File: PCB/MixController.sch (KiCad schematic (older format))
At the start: 20 parts

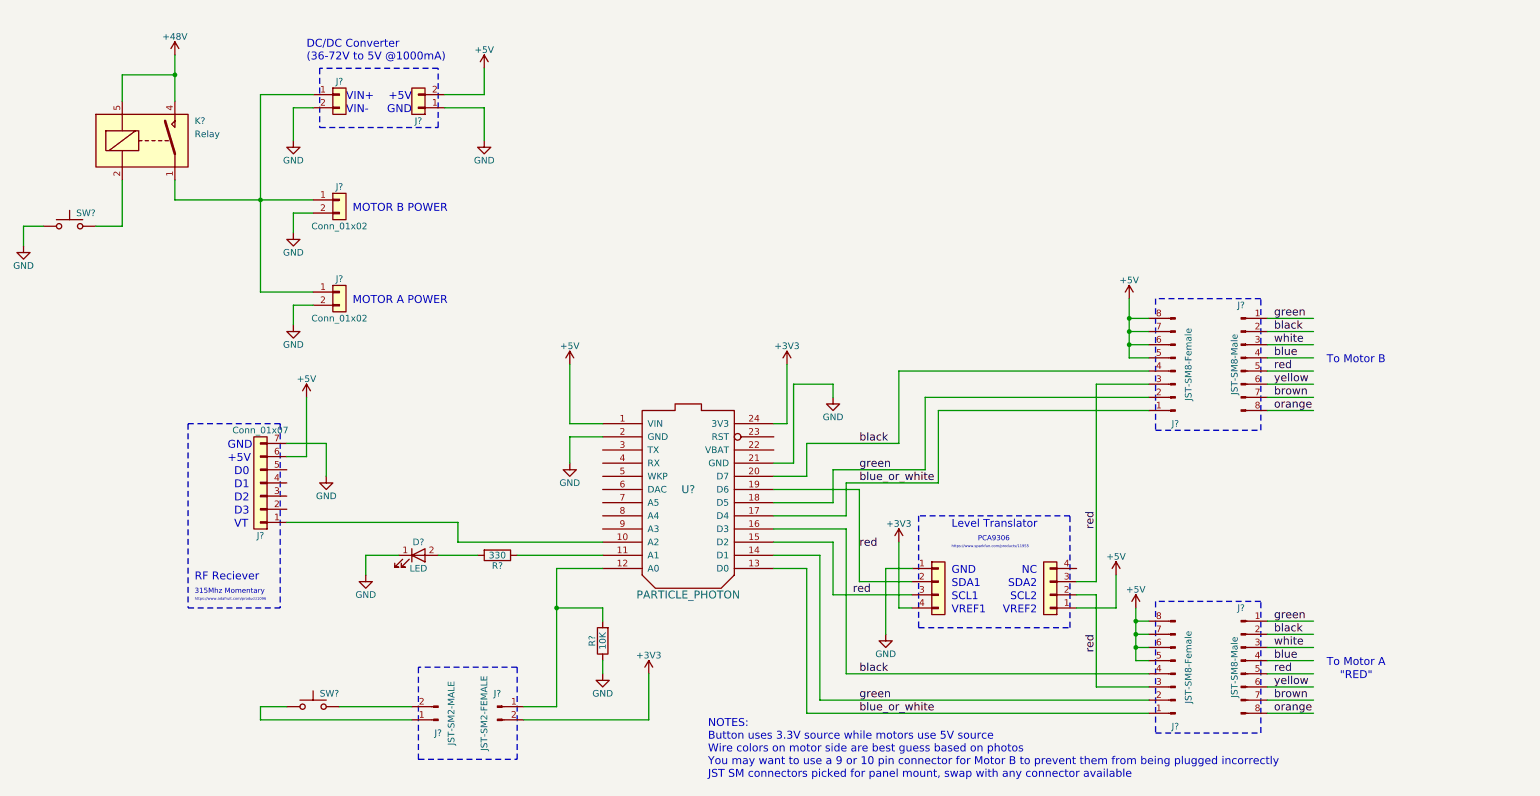
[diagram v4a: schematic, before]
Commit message: Add Level Translators and box image
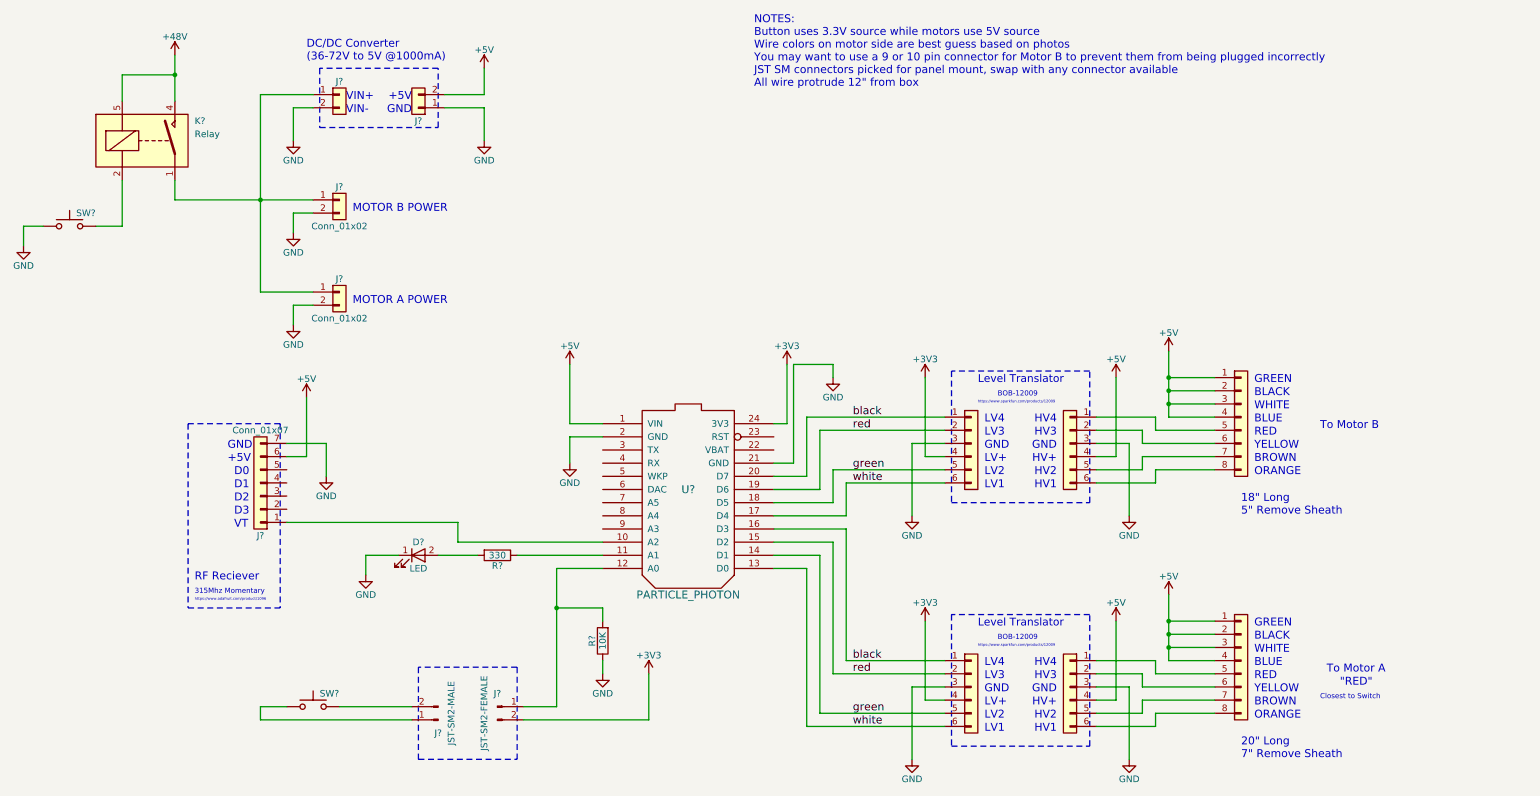
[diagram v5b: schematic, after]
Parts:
- removed J? (x2): JST-SM8-Female, symbol Conn_01x08_Male
- removed J? (x2): JST-SM8-Male, symbol Conn_01x08_Male
- removed J? (x2): Conn_01x04, symbol Conn_01x04
- added J? (x4): Conn_01x06, symbol Conn_01x06
- added J? (x2): Conn_01x08, symbol Conn_01x08
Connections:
- net labels removed: blue, blue_or_white, brown, orange, yellow
- wire segments 123 -> 129
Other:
- note added: "18" Long\n5" Remove Sheath"
- note added: "20" Long\n7" Remove Sheath"
- note added: "BLACK"
- note added: "BLUE"
- note added: "BOB-12009"
- note added: "BROWN"
- note added: "Closest to Switch"
- note added: "GREEN"
- note added: "HV+"
- note added: "HV1"
- note added: "HV2"
- note added: "HV3"
- note added: "HV4"
- note added: "LV+"
- note added: "LV1"
- note added: "LV2"
- note added: "LV3"
- note added: "LV4"
- note added: "NOTES:\nButton uses 3.3V source while motors use 5V source\nWire colors on motor side are best guess based on photos\nYou may want to use a 9 or 10 pin connector for Motor B to prevent them from being plugged incorrectly\nJST SM connectors picked for panel mount, swap with any connector available\nAll wire protrude 12" from box"
- note added: "ORANGE"
- note added: "RED"
- note added: "WHITE"
- note added: "YELLOW"
- note added: "https://www.sparkfun.com/products/12009"
- note removed: "NC"
- note removed: "NOTES:\nButton uses 3.3V source while motors use 5V source\nWire colors on motor side are best guess based on photos\nYou may want to use a 9 or 10 pin connector for Motor B to prevent them from being plugged incorrectly\nJST SM connectors picked for panel mount, swap with any connector available"
- note removed: "PCA9306"
- note removed: "SCL1"
- note removed: "SCL2"
- note removed: "SDA1"
- note removed: "SDA2"
- note removed: "VREF1"
- note removed: "VREF2"
- note removed: "https://www.sparkfun.com/products/11955"

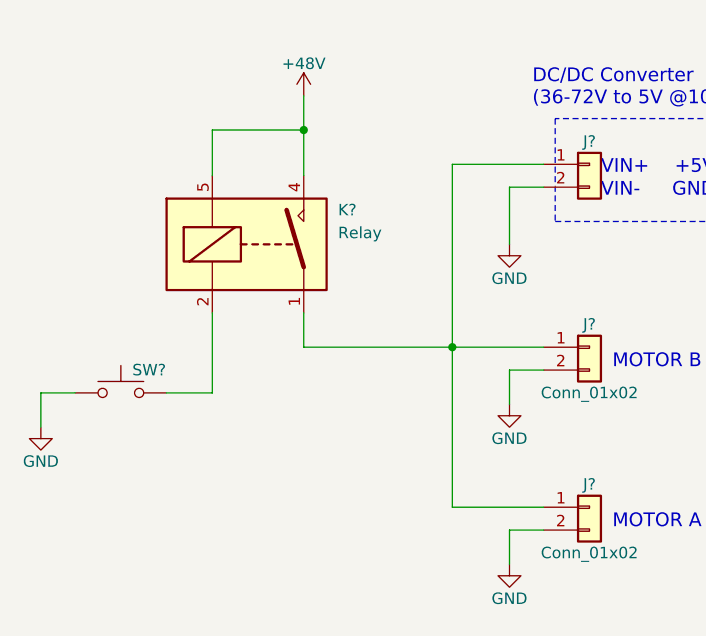
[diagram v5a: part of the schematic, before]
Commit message: Remove Switch and Relay, add Battery Connector
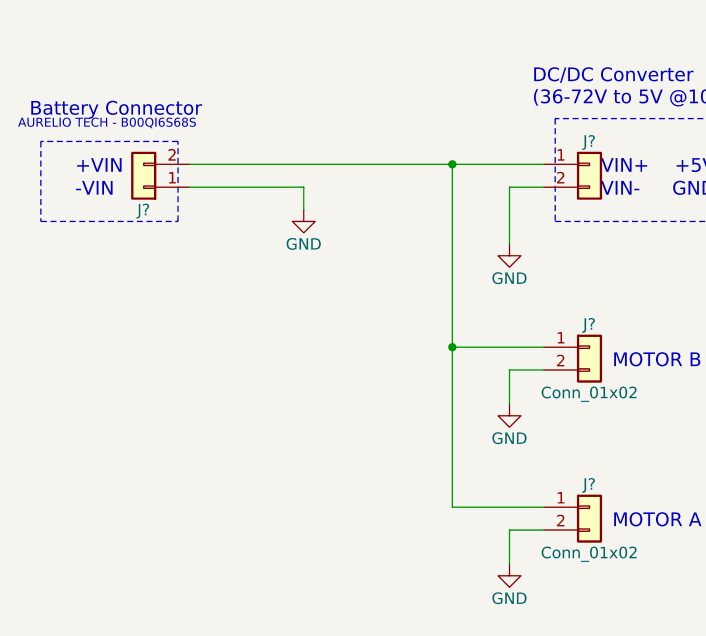
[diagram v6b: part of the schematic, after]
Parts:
- removed K?: Relay, Relays_THT:Relay_SPDT_SANYOU_SRD_Series_Form_A, symbol SANYOU_SRD_Form_A
- removed SW?: SW_Push, symbol SW_Push
- added J?: Conn_01x02, symbol Conn_01x02
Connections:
- net GND: now also J?.1 (Pin_1)
- net at J?.1 (Pin_1), J?.1 (Pin_1), J?.1 (Pin_1): now also J?.2 (Pin_2)
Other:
- note added: "+VIN"
- note added: "-VIN"
- note added: "AURELIO TECH - B00QI6S68S"
- note added: "Battery Connector"
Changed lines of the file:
@@
 red
 $Comp
-L +48V #PWR?
-U 1 1 5B0684B5
-P 1900 800
-F 0 "#PWR?" H 1900 650 50  0001 C CNN
-F 1 "+48V" H 1900 940 50  0000 C CNN
-F 2 "" H 1900 800 50  0001 C CNN
-F 3 "" H 1900 800 50  0001 C CNN
-	1    1900 800
-	1    0    0    -1
-$EndComp
-$Comp
-L SANYOU_SRD_Form_A K?
-U 1 1 5B0686B1
-P 1700 1450
-F 0 "K?" H 2050 1600 50  0000 L CNN
-F 1 "Relay" H 2050 1500 50  0000 L CNN
-F 2 "Relays_THT:Relay_SPDT_SANYOU_SRD_Series_Form_A" H 2950 1400 50  0001 C CNN
-F 3 "" H 1700 1450 50  0001 C CNN
-	1    1700 1450
-	1    0    0    -1
-$EndComp
-$Comp
-L SW_Push SW?
-U 1 1 5B0687B7
-P 1100 2100
-F 0 "SW?" H 1150 2200 50  0000 L CNN
-F 1 "SW_Push" H 1100 2040 50  0001 C CNN
-F 2 "" H 1100 2300 50  0001 C CNN
-F 3 "" H 1100 2300 50  0001 C CNN
-	1    1100 2100
-	1    0    0    -1
-$EndComp
-$Comp
-L GND #PWR?
-U 1 1 5B068C6B
-P 750 2250
-F 0 "#PWR?" H 750 2000 50  0001 C CNN
-F 1 "GND" H 750 2100 50  0000 C CNN
-F 2 "" H 750 2250 50  0001 C CNN
-F 3 "" H 750 2250 50  0001 C CNN
-	1    750  2250
-	1    0    0    -1
-$EndComp
-$Comp
 L Conn_01x02 J?
 U 1 1 5B069086
@@
 	3900 900  3000 900
 Wire Wire Line
-	2550 1100 2950 1100
+	1400 1100 2950 1100
 Wire Wire Line
 	3950 1100 4250 1100
@@
 	2550 1100 2550 2600
 Wire Wire Line
-	1300 2100 1500 2100
-Wire Wire Line
-	1500 2100 1500 1750
-Wire Wire Line
-	900  2100 750  2100
-Wire Wire Line
-	750  2100 750  2250
-Wire Wire Line
 	2950 2700 2800 2700
 Wire Wire Line
@@
 	2800 2000 2800 2150
 Wire Wire Line
-	1900 800  1900 1150
-Wire Wire Line
-	1900 950  1500 950
-Wire Wire Line
-	1500 950  1500 1150
-Connection ~ 1900 950
-Wire Wire Line
 	2950 1200 2800 1200
 Wire Wire Line
 	2800 1200 2800 1450
 Wire Wire Line
-	1900 1900 2950 1900
-Wire Wire Line
 	2550 2600 2950 2600
 Connection ~ 2550 1900
-Wire Wire Line
-	1900 1750 1900 1900
 Wire Notes Line
 	2700 3600 2700 5000
@@
 Text Notes 10600 5700 0    39   ~ 0
 Closest to Switch
+$Comp
+L Conn_01x02 J?
+U 1 1 5B7E7A55
+P 1200 1200
+F 0 "J?" H 1200 1300 50  0000 C CNN
+F 1 "Conn_01x02" H 1200 1000 50  0001 C CNN
+F 2 "" H 1200 1200 50  0001 C CNN
+F 3 "" H 1200 1200 50  0001 C CNN
+	1    1200 1200
+	-1   0    0    1
+$EndComp
+Text Notes 900  1150 0    60   ~ 0
++VIN
+Text Notes 900  1250 0    60   ~ 0
+-VIN
+$Comp
+L GND #PWR?
+U 1 1 5B7E7C43
+P 1900 1300
+F 0 "#PWR?" H 1900 1050 50  0001 C CNN
+F 1 "GND" H 1900 1150 50  0000 C CNN
+F 2 "" H 1900 1300 50  0001 C CNN
+F 3 "" H 1900 1300 50  0001 C CNN
+	1    1900 1300
+	1    0    0    -1
+$EndComp
+Wire Wire Line
+	1900 1300 1900 1200
+Wire Wire Line
+	1900 1200 1400 1200
+Connection ~ 2550 1100
+Wire Wire Line
+	2950 1900 2550 1900
+Wire Notes Line
+	1350 1350 1350 1000
+Wire Notes Line
+	1350 1000 750  1000
+Wire Notes Line
+	750  1000 750  1350
+Wire Notes Line
+	750  1350 1350 1350
+Text Notes 700  900  0    60   ~ 0
+Battery Connector
+Text Notes 650  950  0    39   ~ 0
+AURELIO TECH - B00QI6S68S
 $EndSCHEMATC

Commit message: Add cable notes
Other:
- note added: "15" BLACK 12 AWG"
- note added: "15" RED 12 AWG"
- note added: "18" Long\n5" Remove Sheath\nCut BLACK wire to 2""
- note added: "18" Long\n5" Remove Sheath\nCut RED wire to 2""
- note added: "Same side as +VIN \n(RED)"
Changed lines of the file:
@@
 Text Notes 650  950  0    39   ~ 0
 AURELIO TECH - B00QI6S68S
+Text Notes 10550 5850 0    39   ~ 0
+Same side as +VIN \n(RED)
+Text Notes 4100 2050 0    60   ~ 0
+18" Long\n5" Remove Sheath\nCut BLACK wire to 2"
+Text Notes 4100 2750 0    60   ~ 0
+18" Long\n5" Remove Sheath\nCut RED wire to 2"
+Text Notes 1500 1100 0    60   ~ 0
+15" RED 12 AWG
+Text Notes 1500 1200 0    60   ~ 0
+15" BLACK 12 AWG
 $EndSCHEMATC

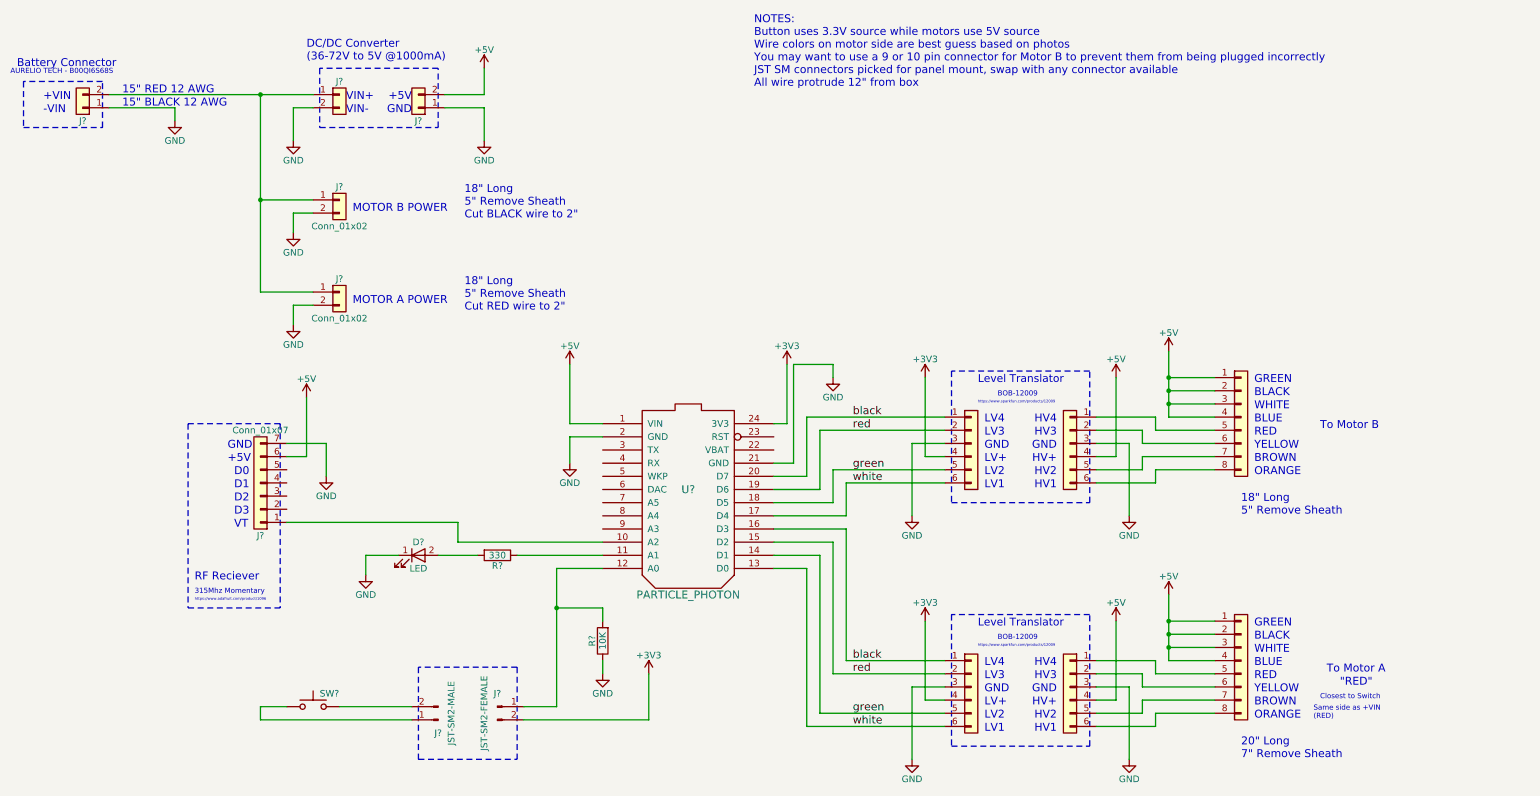
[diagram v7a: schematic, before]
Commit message: Add Rotary Selector
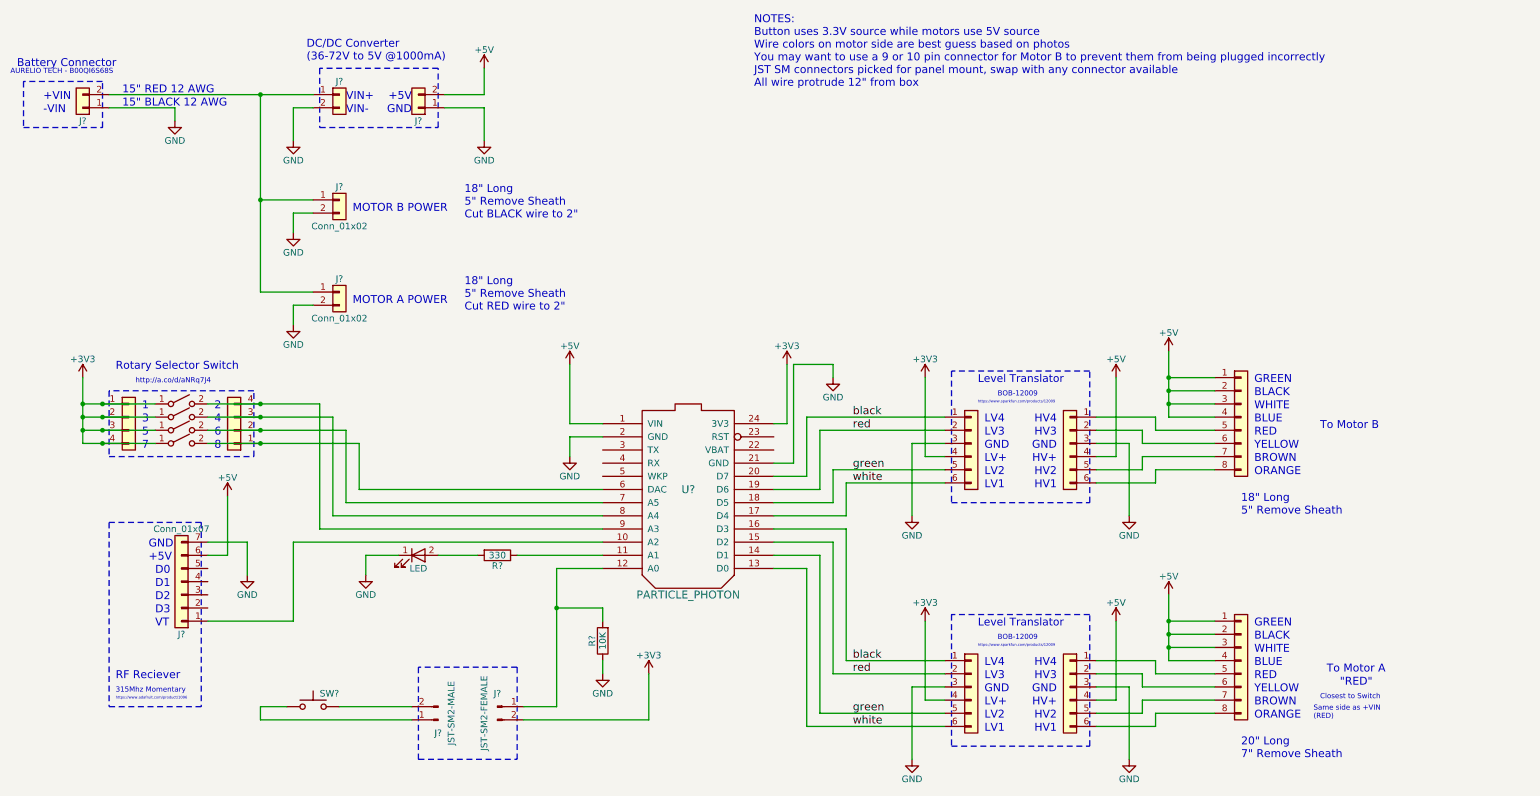
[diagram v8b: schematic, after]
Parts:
- added J? (x2): Conn_01x04, symbol Conn_01x04
- added SW? (x4): SW_SPST, symbol SW_SPST
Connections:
- net +3V3: now also J?.1 (Pin_1), J?.2 (Pin_2), J?.3 (Pin_3), J?.4 (Pin_4), SW?.1 (A), SW?.1 (A), SW?.1 (A), SW?.1 (A)
- net at U?.6 (DAC): now also J?.1 (Pin_1), SW?.2 (B)
- net at U?.7 (A5): now also J?.2 (Pin_2), SW?.2 (B)
- net at U?.8 (A4): now also J?.3 (Pin_3), SW?.2 (B)
- net at U?.9 (A3): now also J?.4 (Pin_4), SW?.2 (B)
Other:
- note added: "1"
- note added: "2"
- note added: "3"
- note added: "4"
- note added: "5"
- note added: "6"
- note added: "7"
- note added: "8"
- note added: "Rotary Selector Switch"
- note added: "http://a.co/d/aNRq7J4"
- moved on the sheet: J?
